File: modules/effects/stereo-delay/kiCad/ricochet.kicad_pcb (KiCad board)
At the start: 2 copper layers, 60 x 110 mm, 129 parts, among them J1 INPUT, J2 OUTPUT, J3 OUTPUT, J4 INPUT, Q1 2N3904, Q2 2N3904, U1 TL072, U2 PT2399, U3 PT2399, U4 TL074, U6 L7805

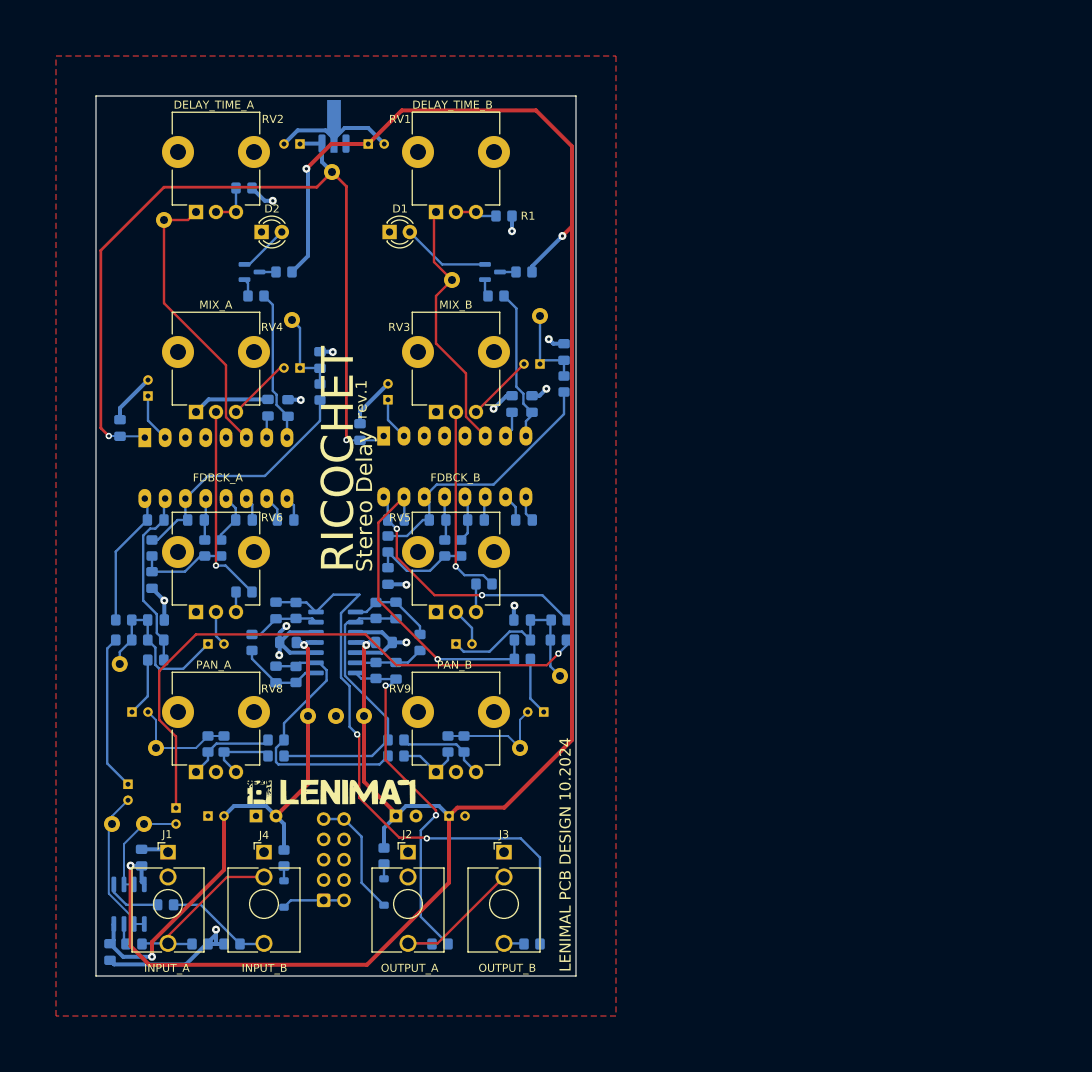
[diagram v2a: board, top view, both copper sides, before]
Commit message: debugging and rework for ricochet, midas, wolkje. Added IBOM for drums and other modules.
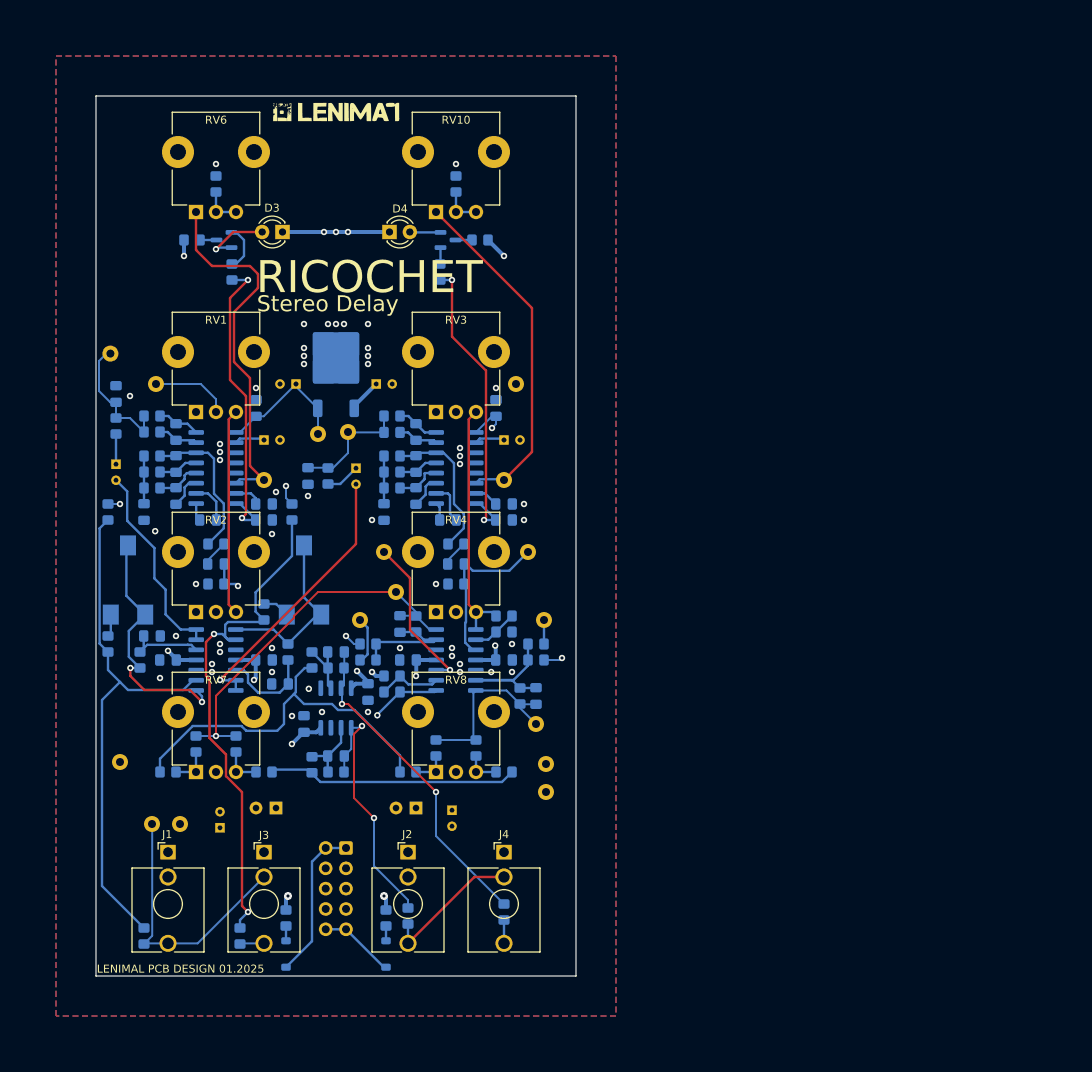
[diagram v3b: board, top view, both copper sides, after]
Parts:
- removed C43: 10uF, Capacitor_THT:CP_Radial_D4.0mm_P2.00mm
- removed C44: 4.7uF, Capacitor_THT:CP_Radial_D4.0mm_P2.00mm
- removed the G*** at (79.5, 137.0)
- added G***: LOGO, Synth:lenimal_logo_full, F.Cu at (80.1, 52.0)
- added G***: LOGO, Synth:lenimal_logo_full, B.Cu at (101.7, 51.5)
- added R47: 10K, Resistor_SMD:R_0805_2012Metric_Pad1.20x1.40mm_HandSolder, B.Cu at (55.5, 120.5)
- added R48: 10K, Resistor_SMD:R_0805_2012Metric_Pad1.20x1.40mm_HandSolder, B.Cu at (87.0, 90.0)
- added R49: 10K, Resistor_SMD:R_0805_2012Metric_Pad1.20x1.40mm_HandSolder, B.Cu at (87.0, 92.0)
- added R50: 10K, Resistor_SMD:R_0805_2012Metric_Pad1.20x1.40mm_HandSolder, B.Cu at (95.0, 106.0)
- added R51: 2K7, Resistor_SMD:R_0805_2012Metric_Pad1.20x1.40mm_HandSolder, B.Cu at (95.0, 61.0)
- added R52: 10K, Resistor_SMD:R_0805_2012Metric_Pad1.20x1.40mm_HandSolder, B.Cu at (87.0, 99.0)
- added R53: 10K, Resistor_SMD:R_0805_2012Metric_Pad1.20x1.40mm_HandSolder, B.Cu at (87.0, 97.0)
- added R54: 15K, Resistor_SMD:R_0805_2012Metric_Pad1.20x1.40mm_HandSolder, B.Cu at (87.0, 95.0)
- added R55: 1K, Resistor_SMD:R_0805_2012Metric_Pad1.20x1.40mm_HandSolder, B.Cu at (93.0, 72.0)
- added R56: 680R, Resistor_SMD:R_0805_2012Metric_Pad1.20x1.40mm_HandSolder, B.Cu at (98.0, 68.0)
- added RV10: B100K, Synth:Potentiometer_TT_P0915N, F.Cu at (95.0, 57.0)
- added RV7: B10K, Synth:Potentiometer_TT_P0915N, F.Cu at (65.0, 127.0)
- added TP15: -12V, Connector_Pin:Pin_D1.0mm_L10.0mm, B.Cu at (53.0, 133.2)
- added TP16: +5V, Connector_Pin:Pin_D1.0mm_L10.0mm, B.Cu at (77.8, 92.2)
- added TP17: DELAY_TIME, Connector_Pin:Pin_D1.0mm_L10.0mm, B.Cu at (71.0, 98.0)
- added TP18: DELAY_TIME, Connector_Pin:Pin_D1.0mm_L10.0mm, B.Cu at (101.0, 98.0)
- added U5: PT2399, Synth:SOIC-16, B.Cu at (65.0, 96.5)
- C1: value 10uF -> 1uF; footprint Capacitor_THT:CP_Radial_D4.0mm_P2.00mm -> Capacitor_SMD:C_0805_2012Metric_Pad1.18x1.45mm_HandSolder
- C10, C6, C7, C8: footprint Capacitor_SMD:C_0805_2012Metric_Pad1.18x1.45mm_HandSolder -> Capacitor_THT:CP_Radial_D4.0mm_P2.00mm
- C11, C13, C16: value 560pF -> 100nF
- C15, C20: value 4.7uF -> 100nF; footprint Capacitor_THT:CP_Radial_D4.0mm_P2.00mm -> Capacitor_SMD:C_0805_2012Metric_Pad1.18x1.45mm_HandSolder
- C17: value 4.7uF -> 1uF
- C18: value 560pF -> 1nF
- C19: value 3.3nF -> 2.2nF
- C2, C29, C30: value 100nF -> 47pF
- C21: value 10uF -> 560pF; footprint Capacitor_THT:CP_Radial_D4.0mm_P2.00mm -> Capacitor_SMD:C_0805_2012Metric_Pad1.18x1.45mm_HandSolder
- C22: value 3.3nF -> 1uF; footprint Capacitor_SMD:C_0805_2012Metric_Pad1.18x1.45mm_HandSolder -> Capacitor_THT:CP_Radial_D4.0mm_P2.00mm
- C23: value 10nF -> 2.2nF
- C24, C39: value 3.9nF -> 100nF
- C25, C26: value 27pF -> 100nF
- C27: value 47pF -> 100nF
- C28: value 47pF -> 3.3nF
- C3, C36: value 100nF -> 1uF
- C31: value 47uF -> 1uF; footprint Capacitor_THT:CP_Radial_D6.3mm_P2.50mm -> Capacitor_THT:CP_Radial_D4.0mm_P2.00mm
- C32: value 47uF -> 1nF; footprint Capacitor_THT:CP_Radial_D6.3mm_P2.50mm -> Capacitor_SMD:C_0805_2012Metric_Pad1.18x1.45mm_HandSolder
- C33: value 100nF -> 2.2nF
- C35: value 100nF -> 560pF; footprint Capacitor_THT:CP_Radial_D4.0mm_P2.00mm -> Capacitor_SMD:C_0805_2012Metric_Pad1.18x1.45mm_HandSolder
- C37: value 100nF -> 2.2nF; footprint Capacitor_THT:CP_Radial_D4.0mm_P2.00mm -> Capacitor_SMD:C_0805_2012Metric_Pad1.18x1.45mm_HandSolder
- C38: footprint Capacitor_THT:CP_Radial_D4.0mm_P2.00mm -> Capacitor_SMD:C_0805_2012Metric_Pad1.18x1.45mm_HandSolder
- C4: value 10uF -> 47pF; footprint Capacitor_THT:CP_Radial_D4.0mm_P2.00mm -> Capacitor_SMD:C_0805_2012Metric_Pad1.18x1.45mm_HandSolder
- C40: value 10nF -> 100nF
- C41: value 10uF -> 100nF; footprint Capacitor_THT:CP_Radial_D4.0mm_P2.00mm -> Capacitor_SMD:C_0805_2012Metric_Pad1.18x1.45mm_HandSolder
- C42: value 10uF -> 3.3nF; footprint Capacitor_THT:CP_Radial_D4.0mm_P2.00mm -> Capacitor_SMD:C_0805_2012Metric_Pad1.18x1.45mm_HandSolder
- C5, C9: value 100nF -> 47uF; footprint Capacitor_SMD:C_0805_2012Metric_Pad1.18x1.45mm_HandSolder -> Capacitor_THT:CP_Radial_D6.3mm_P2.50mm
- D1, D2: value LED -> 1N5819; footprint Synth:LED_D3.0mm -> Diode_SMD:D_SOD-123; moved to B.Cu
- D3, D4: value 1N5819 -> LED; footprint Diode_SMD:D_SOD-123 -> Synth:LED_D3.0mm; moved to F.Cu
- R1: value 2K -> 100K
- R10: value 15K -> 82K
- R12, R19: value 5.6K -> 100K
- R13: value 15K -> 100K
- R14, R17, R9: value 10K -> 100K
- R15, R16: value 10K -> 10R
- R18: value 4.7K -> 5K6
- R2: value 2K -> 82K
- R20, R21: value 15K -> 10K
- R23, R4: value 1K -> 10K
- R24: value 100K -> 10K
- R25: value 10K -> 2K7
- R27: value 4.7K -> 10K
- R28: value 10K -> 15K
- R29: value 10K -> 1K
- R30: value 10K -> 680R
- R37, R38: value 33K -> 10K
- R43, R5, R6: value 1K -> 100K
- R44: value 1K -> 5K6
- R45: value 10R -> 100K
- R46: value 10R -> 10K
- R7, R8: value 680R -> 1K
- RV1, RV2: value B50K -> B10K
- RV3, RV4: value B100K -> B10K
- RV5: value B100K -> 10K; footprint Synth:Potentiometer_TT_P0915N -> Potentiometer_SMD:Potentiometer_ACP_CA6-VSMD_Vertical; moved to B.Cu
- RV9: value B10K -> 10K; footprint Synth:Potentiometer_TT_P0915N -> Potentiometer_SMD:Potentiometer_ACP_CA6-VSMD_Vertical; moved to B.Cu
- TP1: value +12V -> FEEDBACK_A
- TP10: value POST_FEEDBACK_CH_2 -> OUTPUT_CH_1
- TP11: value POST_FEEDBACK_CH_1 -> MIXED_OUT_B
- TP12: value MIX_INPUT_CH_2 -> WET_OUT_B
- TP13: value MIX_INPUT_CH_1 -> +12V
- TP14: value +5V -> GND
- TP2: value GND -> DRY_A
- TP3: value -12V -> INPUT_CH_1
- TP4: value INPUT_CH_1 -> OUTPUT_CH_1
- TP5: value INPUT_CH_2 -> WET_OUT_A
- TP6: value OUTPUT_CH_1 -> FEEDBACK_B
- TP7: value OUTPUT_CH_2 -> MIXED_OUT_A
- TP8: value DELAY_TIME_CH_2 -> DRY_B
- TP9: value DELAY_TIME_CH_1 -> INPUT_CH_2
- U1: value TL072 -> TL074; footprint Synth:SOIC-8 -> Synth:SOIC-14
- U2: value PT2399 -> L7805; footprint Package_DIP:DIP-16_W7.62mm_Socket_LongPads -> Package_TO_SOT_SMD:TO-252-2
- U3: value PT2399 -> TL074; footprint Package_DIP:DIP-16_W7.62mm_Socket_LongPads -> Synth:SOIC-14
- U4: value TL074 -> TL072; footprint Synth:SOIC-14 -> Synth:SOIC-8
- U6: value L7805 -> PT2399; footprint Package_TO_SOT_SMD:SOT-89-3_Handsoldering -> Synth:SOIC-16
- moved D1 90.3 mm to (86.2, 157.2), turned to -90 degrees
- moved D2 90.3 mm to (73.8, 157.2), turned to 90 degrees
- moved R8 84.6 mm to (101.0, 152.0), turned to 90 degrees
- moved D4 84.0 mm to (88.0, 67.0), turned to 0 degrees
- moved D3 83.7 mm to (72.0, 67.0), turned to 180 degrees
- moved R7 81.8 mm to (89.0, 152.5), turned to 90 degrees
- moved TP14 78.7 mm to (106.2, 133.5)
- moved TP8 76.0 mm to (60.5, 141.0)
- moved R19 68.7 mm to (68.0, 155.0), turned to -90 degrees
- moved R43 68.1 mm to (51.5, 102.0), turned to 90 degrees
- moved TP13 67.0 mm to (106.2, 137.0)
- moved R2 65.7 mm to (87.0, 124.5), turned to 0 degrees
- moved R44 64.9 mm to (51.5, 118.5), turned to -90 degrees
- moved TP6 64.0 mm to (102.5, 86.0)
- moved R30 63.0 mm to (62.0, 68.0), turned to 180 degrees
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- renumbered J4 to J3, J3 to J4
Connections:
- C1 pad 1: Net-(U2-REF) -> /delay_stage_A/DELAY_OUT
- C1 pad 2: GNDREF -> Net-(U1C-+)
- C10 pad 1: Net-(U3-OP2-IN) -> GNDREF
- C10 pad 2: Net-(U3-OP2-OUT) -> -12V
- C11 pad 1: Net-(U2-LPF1-IN) -> +12V
- C11 pad 2: Net-(U2-LPF1-OUT) -> GNDREF
- C12 pad 1: Net-(U3-OP1-IN) -> +12V
- C12 pad 2: Net-(U3-OP1-OUT) -> GNDREF
- C13 pad 1: Net-(U2-LPF2-OUT) -> +12V
- C13 pad 2: Net-(U2-LPF2-IN) -> GNDREF
- C14 pad 1: Net-(U2-OP2-IN) -> GNDREF
- C14 pad 2: Net-(U2-OP2-OUT) -> -12V
- C15 pad 1: Net-(C15-Pad1) -> GNDREF
- C15 pad 2: /PT2399_delay-module_channel_1/delay_input -> -12V
- C16 pad 1: Net-(U3-LPF1-IN) -> GNDREF
- C16 pad 2: Net-(U3-LPF1-OUT) -> -12V
- C17 pad 2: /PT2399_delay-module_channel_2/delay_input -> Net-(U3B--)
- C18 pad 1: Net-(U3-LPF2-OUT) -> GNDREF
- C18 pad 2: Net-(U3-LPF2-IN) -> /delay_stage_B/DELAY_IN
- C19 pad 1: Net-(C19-Pad1) -> GNDREF
- C19 pad 2: GNDREF -> Net-(U3B-+)
- C2 pad 1: GNDREF -> Net-(U1D--)
- C2 pad 2: +5V -> /panning/INPUT_A
- C20 pad 1: Net-(C20-Pad1) -> GNDREF
- C20 pad 2: Net-(C20-Pad2) -> +5V
- C21 pad 1: Net-(C21-Pad1) -> Net-(U5-LPF1-IN)
- C21 pad 2: Net-(C21-Pad2) -> Net-(U5-LPF1-OUT)
- C22 pad 1: Net-(C22-Pad1) -> Net-(U5-REF)
- C23 pad 1: Net-(C23-Pad1) -> Net-(U5-LPF2-OUT)
- C23 pad 2: GNDREF -> Net-(U5-LPF2-IN)
- C24 pad 1: Net-(C24-Pad1) -> Net-(U5-OP2-OUT)
- C24 pad 2: GNDREF -> Net-(U5-OP2-IN)
- C25 pad 1: Net-(U4A--) -> GNDREF
- C25 pad 2: Net-(C25-Pad2) -> Net-(U5-CC1)
- C26 pad 1: Net-(U4C--) -> Net-(U5-CC0)
- C26 pad 2: Net-(C26-Pad2) -> GNDREF
- C27 pad 1: Net-(U4B--) -> Net-(U5-OP1-IN)
- C27 pad 2: Net-(C27-Pad2) -> Net-(U5-OP1-OUT)
- C28 pad 1: Net-(U4D--) -> Net-(C28-Pad1)
- C28 pad 2: Net-(C28-Pad2) -> GNDREF
- C29 pad 1: +12V -> Net-(U4A--)
- C29 pad 2: GNDREF -> /panning/OUTPUT_A
- C3 pad 1: Net-(U2-CC1) -> /delay_stage_B/DELAY_OUT
- C3 pad 2: GNDREF -> Net-(U1A-+)
- C30 pad 1: GNDREF -> Net-(U4B--)
- C30 pad 2: -12V -> /panning/OUTPUT_B
- C31 pad 1: +12V -> Net-(C31-Pad1)
- C31 pad 2: GNDREF -> Net-(U3D--)
- C32 pad 2: -12V -> /delay_stage_A/DELAY_IN
- C33 pad 1: +12V -> GNDREF
- C33 pad 2: GNDREF -> Net-(U3D-+)
- C34 pad 2: -12V -> +5V
- C35 pad 1: +12V -> Net-(U6-LPF1-IN)
- C35 pad 2: GNDREF -> Net-(U6-LPF1-OUT)
- C36 pad 1: GNDREF -> Net-(U6-REF)
- C36 pad 2: -12V -> GNDREF
- C37 pad 1: +12V -> Net-(U6-LPF2-OUT)
- C37 pad 2: GNDREF -> Net-(U6-LPF2-IN)
- C38 pad 1: +5V -> Net-(U6-OP2-OUT)
- C38 pad 2: GNDREF -> Net-(U6-OP2-IN)
- C39 pad 1: Net-(C20-Pad1) -> GNDREF
- C39 pad 2: GNDREF -> Net-(U6-CC1)
- C4 pad 1: Net-(U3-REF) -> Net-(U1B--)
- C4 pad 2: GNDREF -> /panning/INPUT_B
- C40 pad 1: Net-(C21-Pad1) -> Net-(U6-CC0)
- C41 pad 1: Net-(C41-Pad1) -> Net-(U6-OP1-IN)
- C41 pad 2: /PT2399_delay-module_channel_2/delay_output -> Net-(U6-OP1-OUT)
- C42 pad 2: /PT2399_delay-module_channel_1/delay_output -> GNDREF
- C5 pad 1: Net-(U2-CC0) -> +12V
- C6 pad 1: +5V -> +12V
- C7 pad 1: Net-(U3-CC1) -> +12V
- C8 pad 1: Net-(U3-CC0) -> +5V
- C9 pad 1: Net-(U2-OP1-IN) -> GNDREF
- C9 pad 2: Net-(U2-OP1-OUT) -> -12V
- D1 pad 1: GNDREF -> Net-(D1-K)
- D2 pad 1: GNDREF -> Net-(D2-K)
- D3 pad 1: Net-(D3-K) -> GNDREF
- D4 pad 1: Net-(D4-K) -> GNDREF
- H1 pad 1: Net-(D4-K) -> Net-(D2-K)
- H1 pad 10: Net-(D3-A) -> Net-(D1-A)
- H1 pad 2: Net-(D4-K) -> Net-(D2-K)
- H1 pad 9: Net-(D3-A) -> Net-(D1-A)
- J1 pad T: Net-(J1-PadT) -> /input_stage_A/DRY_IN
- J3 pad T: Net-(J4-PadT) -> /input_stage_B/DRY_IN
- J3 pad TN: Net-(J1-PadT) -> /input_stage_A/DRY_IN
- J4 pad T: Net-(J3-PadT) -> Net-(J4-PadT)
- Q1 pad 2: Net-(D1-A) -> Net-(D3-A)
- Q2 pad 2: Net-(D2-A) -> Net-(D4-A)
- R1 pad 2: Net-(R1-Pad2) -> Net-(U1C-+)
- R10 pad 1: Net-(C15-Pad1) -> Net-(U1A--)
- R10 pad 2: Net-(C24-Pad1) -> Net-(R10-Pad2)
- R11 pad 1: Net-(U2-LPF1-OUT) -> GNDREF
- R11 pad 2: Net-(C20-Pad1) -> Net-(U1A--)
- R12 pad 1: Net-(U2-LPF2-OUT) -> Net-(U1B--)
- R12 pad 2: Net-(C21-Pad1) -> /panning/INPUT_B
- R13 pad 1: Net-(U2-LPF2-OUT) -> Net-(R13-Pad1)
- R13 pad 2: Net-(C19-Pad1) -> Net-(U1B--)
- R14 pad 1: Net-(U2-LPF2-IN) -> /input_stage_B/DRY_IN
- R14 pad 2: Net-(C19-Pad1) -> Net-(U1B--)
- R15 pad 1: Net-(U2-OP2-OUT) -> Net-(D1-K)
- R15 pad 2: Net-(C19-Pad1) -> +12V
- R16 pad 1: Net-(U3-LPF1-IN) -> Net-(D2-A)
- R16 pad 2: Net-(C24-Pad1) -> -12V
- R17 pad 1: Net-(U3-LPF1-OUT) -> Net-(U3A--)
- R17 pad 2: Net-(C24-Pad1) -> /input_stage_B/FEEDBACKIN_IN
- R18 pad 1: Net-(U3-LPF1-OUT) -> Net-(R18-Pad1)
- R18 pad 2: Net-(C42-Pad1) -> Net-(U3A--)
- R19 pad 1: Net-(U3-LPF2-OUT) -> Net-(U3A--)
- R19 pad 2: Net-(C23-Pad1) -> /input_stage_B/DRY_IN
- R2 pad 1: GNDREF -> Net-(U1C--)
- R20 pad 1: Net-(U3-LPF2-OUT) -> Net-(C17-Pad1)
- R20 pad 2: Net-(C22-Pad1) -> /delay_stage_B/DELAY_IN
- R21 pad 1: Net-(C17-Pad1) -> Net-(U3B-+)
- R21 pad 2: Net-(C20-Pad1) -> Net-(R21-Pad2)
- R22 pad 1: Net-(U3-LPF2-IN) -> /delay_stage_A/DELAY_IN
- R22 pad 2: Net-(C22-Pad1) -> Net-(U5-LPF1-IN)
- R23 pad 1: Net-(U1B-+) -> /delay_stage_A/DELAY_IN
- R23 pad 2: Net-(J4-PadT) -> Net-(U5-LPF1-OUT)
- R24 pad 1: GNDREF -> Net-(U5-LPF2-OUT)
- R24 pad 2: Net-(J4-PadT) -> /delay_stage_A/DELAY_OUT
- R25 pad 1: Net-(R25-Pad1) -> GNDREF
- R26 pad 1: Net-(U3-OP2-OUT) -> Net-(C28-Pad1)
- R26 pad 2: Net-(C22-Pad1) -> Net-(U5-OP2-OUT)
- R27 pad 1: Net-(U2-LPF1-OUT) -> Net-(C28-Pad1)
- R27 pad 2: Net-(C41-Pad1) -> Net-(U5-LPF2-IN)
- R28 pad 1: Net-(R28-Pad1) -> Net-(C28-Pad1)
- R28 pad 2: Net-(R28-Pad2) -> Net-(U5-LPF2-OUT)
- R29 pad 1: /PT2399_delay-module_channel_1/delay_output -> Net-(U5-CC0)
- R29 pad 2: Net-(R29-Pad2) -> Net-(Q1-B)
- R3 pad 1: GNDREF -> Net-(U1D--)
- R3 pad 2: Net-(J1-PadT) -> /panning/INPUT_A
- R30 pad 1: /PT2399_delay-module_channel_1/delay_output -> Net-(Q1-C)
- R30 pad 2: Net-(R30-Pad2) -> +12V
- R31 pad 1: /PT2399_delay-module_channel_2/delay_output -> Net-(U4A--)
- R31 pad 2: Net-(R31-Pad2) -> /panning/OUTPUT_A
- R32 pad 1: /PT2399_delay-module_channel_2/delay_output -> /panning/INPUT_A
- R33 pad 1: Net-(R29-Pad2) -> Net-(R32-Pad2)
- R33 pad 2: Net-(U4A--) -> Net-(R33-Pad2)
- R34 pad 1: Net-(R30-Pad2) -> Net-(R33-Pad2)
- R34 pad 2: Net-(U4C--) -> Net-(U4A--)
- R35 pad 1: Net-(R31-Pad2) -> /panning/INPUT_A
- R35 pad 2: Net-(U4A--) -> Net-(R35-Pad2)
- R36 pad 1: Net-(R32-Pad2) -> Net-(R36-Pad1)
- R36 pad 2: Net-(U4C--) -> Net-(R35-Pad2)
- R37 pad 1: Net-(U4A--) -> /panning/INPUT_B
- R37 pad 2: Net-(C25-Pad2) -> Net-(R37-Pad2)
- R38 pad 1: Net-(U4C--) -> Net-(R37-Pad2)
- R38 pad 2: Net-(C26-Pad2) -> Net-(R33-Pad2)
- R39 pad 1: Net-(C25-Pad2) -> Net-(U4B--)
- R39 pad 2: Net-(U4B--) -> /panning/OUTPUT_B
- R4 pad 1: Net-(U1A-+) -> GNDREF
- R4 pad 2: Net-(J1-PadT) -> Net-(U1C--)
- R40 pad 1: Net-(C26-Pad2) -> /panning/INPUT_B
- R40 pad 2: Net-(U4D--) -> Net-(R40-Pad2)
- R41 pad 1: Net-(U4B--) -> Net-(R40-Pad2)
- R41 pad 2: Net-(C27-Pad2) -> Net-(R36-Pad1)
- R42 pad 1: Net-(U4D--) -> Net-(R36-Pad1)
- R42 pad 2: Net-(C28-Pad2) -> Net-(U4B--)
- R43 pad 1: Net-(J2-PadT) -> Net-(U3C--)
- R43 pad 2: Net-(C27-Pad2) -> /input_stage_A/FEEDBACKIN_IN
- R44 pad 1: Net-(J3-PadT) -> Net-(R44-Pad1)
- R44 pad 2: Net-(C28-Pad2) -> Net-(U3C--)
- R45 pad 1: Net-(D3-K) -> Net-(U3C--)
- R45 pad 2: +12V -> /input_stage_A/DRY_IN
- R46 pad 1: Net-(D4-A) -> Net-(C31-Pad1)
- R46 pad 2: -12V -> /delay_stage_A/DELAY_IN
- R5 pad 1: Net-(U2-CC0) -> Net-(R5-Pad1)
- R5 pad 2: Net-(Q1-B) -> Net-(U1D--)
- R6 pad 1: Net-(U3-CC0) -> /input_stage_A/DRY_IN
- R6 pad 2: Net-(Q2-B) -> Net-(U1D--)
- R7 pad 1: Net-(Q1-C) -> Net-(J2-PadT)
- R7 pad 2: +12V -> /panning/OUTPUT_A
- R8 pad 1: Net-(Q2-C) -> Net-(J4-PadT)
- R8 pad 2: +12V -> /panning/OUTPUT_B
- R9 pad 1: Net-(U2-LPF1-IN) -> GNDREF
- R9 pad 2: Net-(C20-Pad1) -> Net-(U1A-+)
- RV1 pad 1: Net-(U2-VCO) -> GNDREF
- RV1 pad 2: Net-(R1-Pad2) -> /input_stage_A/FEEDBACKIN_IN
- RV1 pad 3: Net-(R1-Pad2) -> Net-(R2-Pad2)
- RV2 pad 1: Net-(U3-VCO) -> GNDREF
- RV2 pad 2: Net-(R2-Pad2) -> Net-(R5-Pad1)
- RV3 pad 2: Net-(R25-Pad2) -> /input_stage_B/FEEDBACKIN_IN
- RV3 pad 3: Net-(C21-Pad2) -> Net-(R10-Pad2)
- RV4 pad 2: Net-(R28-Pad2) -> Net-(R13-Pad1)
- RV4 pad 3: Net-(C43-Pad2) -> Net-(R10-Pad2)
- RV5 pad 1: unconnected-(RV5-Pad1) -> Net-(R18-Pad1)
- RV5 pad 2: Net-(C20-Pad2) -> Net-(R21-Pad2)
- RV5 pad 3: Net-(R25-Pad1) -> Net-(R21-Pad2)
- RV6 pad 1: unconnected-(RV6-Pad1) -> Net-(U5-VCO)
- RV6 pad 2: Net-(C44-Pad2) -> Net-(R25-Pad2)
- RV6 pad 3: Net-(R28-Pad1) -> Net-(R25-Pad2)
- RV8 pad 1: Net-(R30-Pad2) -> Net-(R40-Pad2)
- RV8 pad 3: Net-(R29-Pad2) -> Net-(R37-Pad2)
- RV9 pad 1: Net-(R32-Pad2) -> Net-(R44-Pad1)
- RV9 pad 2: GNDREF -> Net-(R47-Pad2)
- RV9 pad 3: Net-(R31-Pad2) -> Net-(R47-Pad2)
- TP1 pad 1: +12V -> /input_stage_A/FEEDBACKIN_IN
- TP10 pad 1: Net-(C20-Pad1) -> Net-(U1A-+)
- TP11 pad 1: Net-(C24-Pad1) -> /panning/INPUT_B
- TP12 pad 1: Net-(C21-Pad1) -> Net-(R13-Pad1)
- TP13 pad 1: Net-(C23-Pad1) -> +12V
- TP14 pad 1: +5V -> GNDREF
- TP2 pad 1: GNDREF -> /input_stage_A/DRY_IN
- TP3 pad 1: -12V -> /delay_stage_A/DELAY_IN
- TP4 pad 1: /PT2399_delay-module_channel_1/delay_input -> Net-(U1C-+)
- TP5 pad 1: /PT2399_delay-module_channel_2/delay_input -> Net-(R5-Pad1)
- TP6 pad 1: /PT2399_delay-module_channel_1/delay_output -> /input_stage_B/FEEDBACKIN_IN
- TP7 pad 1: /PT2399_delay-module_channel_2/delay_output -> /panning/INPUT_A
- TP8 pad 1: Net-(U2-VCO) -> /input_stage_B/DRY_IN
- TP9 pad 1: Net-(U3-VCO) -> /delay_stage_B/DELAY_IN
- U1 pad 1: /PT2399_delay-module_channel_1/delay_input -> Net-(R10-Pad2)
- U1 pad 2: /PT2399_delay-module_channel_1/delay_input -> Net-(U1A--)
- U1 pad 4: -12V -> +12V
- U1 pad 5: Net-(U1B-+) -> GNDREF
- U1 pad 6: /PT2399_delay-module_channel_2/delay_input -> Net-(U1B--)
- U1 pad 7: /PT2399_delay-module_channel_2/delay_input -> /panning/INPUT_B
- U1 pad 8: +12V -> Net-(R2-Pad2)
- U2 pad 1: +5V -> +12V
- U2 pad 2: Net-(U2-REF) -> GNDREF
- U2 pad 3: GNDREF -> +5V
- U3 pad 1: +5V -> Net-(R21-Pad2)
- U3 pad 10: Net-(U3-OP1-IN) -> GNDREF
- U3 pad 11: Net-(U3-OP2-IN) -> -12V
- U3 pad 12: Net-(U3-OP2-OUT) -> Net-(U3D-+)
- U3 pad 13: Net-(U3-LPF2-IN) -> Net-(U3D--)
- U3 pad 14: Net-(U3-LPF2-OUT) -> Net-(U3D--)
- U3 pad 2: Net-(U3-REF) -> Net-(U3A--)
- U3 pad 4: GNDREF -> +12V
- U3 pad 5: unconnected-(U3-CLK_O-Pad5) -> Net-(U3B-+)
- U3 pad 6: Net-(U3-VCO) -> Net-(U3B--)
- U3 pad 7: Net-(U3-CC1) -> Net-(U3B--)
- U3 pad 8: Net-(U3-CC0) -> Net-(R47-Pad2)
- U3 pad 9: Net-(U3-OP1-OUT) -> Net-(U3C--)
- U4 pad 1: Net-(C25-Pad2) -> /panning/OUTPUT_A
- U4 pad 4: +12V -> -12V
- U4 pad 7: Net-(C27-Pad2) -> /panning/OUTPUT_B
- U4 pad 8: Net-(C26-Pad2) -> +12V
- U6 pad 1: +12V -> +5V
- U6 pad 2: GNDREF -> Net-(U6-REF)
- U6 pad 3: +5V -> GNDREF
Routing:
- net /input_stage_B/DRY_IN: track 0.00 -> 103.0 mm, vias 0 -> 1
- net GNDREF: track 111.5 -> 15.1 mm, vias 14 -> 55
- net /input_stage_A/DRY_IN: track 0.00 -> 92.0 mm, vias 0 -> 1
- net Net-(C28-Pad2): track 75.6 -> 0.00 mm, vias 2 -> 0
- net Net-(C17-Pad1): track 74.1 -> 4.32 mm, vias 1 -> 0
- net Net-(U3C--): track 0.00 -> 66.0 mm
- net Net-(U3A--): track 0.00 -> 64.7 mm, vias 0 -> 2
- net Net-(R2-Pad2): track 5.50 -> 64.6 mm, vias 0 -> 1
- net +5V: track 107.1 -> 49.2 mm, vias 2 -> 1
- net /panning/INPUT_A: track 0.00 -> 47.3 mm, vias 0 -> 1
- net Net-(R36-Pad1): track 0.00 -> 46.9 mm
- net Net-(U5-VCO): track 0.00 -> 46.1 mm
- net Net-(U1C-+): track 0.00 -> 44.3 mm, vias 0 -> 2
- net Net-(C27-Pad2): track 44.1 -> 0.00 mm, vias 2 -> 0
- net Net-(U6-VCO): track 0.00 -> 43.7 mm
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- added copper zone on B.Cu, net GNDREF
- added copper zone on In1.Cu, net GNDREF
- added copper zone on In2.Cu, net GNDREF
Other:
- copper layers 2 -> 4
- board text added: "+12V"
- board text added: "-12V"
- board text added: "A_AMT"
- board text added: "B_AMT"
- board text added: "DLY_A"
- board text added: "DLY_B"
- board text added: "DLY_IN_A"
- board text added: "DLY_IN_B"
- board text added: "DRY_A"
- board text added: "DRY_B"
- board text added: "FBK_A"
- board text added: "FBK_B"
- board text added: "GND"
- board text added: "LENIMAL PCB DESIGN 01.2025"
- board text added: "WET_A"
- board text added: "WET_B"
- board text removed: "DELAY_TIME"
- board text removed: "DELAY_TIME_A"
- board text removed: "DELAY_TIME_B"
- board text removed: "DLY_IN"
- board text removed: "DLY_OUT"
- board text removed: "FDBCK"
- board text removed: "FDBCK_A"
- board text removed: "FDBCK_B"
- board text removed: "INPUT_A"
- board text removed: "INPUT_B"
- board text removed: "L7805"
- board text removed: "LENIMAL PCB DESIGN 10.2024"
- board text removed: "MIX"
- board text removed: "OUTPUT_A"
- board text removed: "OUTPUT_B"
- board text removed: "PAN_A"
- board text removed: "PAN_B"
- board text removed: "PT2399"
- board text removed: "TL072"
- board text removed: "TL074"
- board text removed: "rev.1"

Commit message: Add: Quantizer init, Fix: Stereo-Delay, Fix: Midi-2-xc
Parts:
- C18, C32: value 1nF -> 4.7nF
- C7, C8: value 100nF -> 10uF
- R13, R5: value 100K -> 68K
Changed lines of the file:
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@@
 			)
 		)
-		(property "Value" "100nF"
+		(property "Value" "10uF"
 			(at 1 -3.25 0)
 			(layer "B.Fab")
@@
 			)
 		)
-		(property "Value" "100nF"
+		(property "Value" "10uF"
 			(at 1 -3.25 0)
 			(layer "B.Fab")
@@
 			)
 		)
-		(property "Value" "1nF"
+		(property "Value" "4.7nF"
 			(at 0 -1.68 90)
 			(layer "B.Fab")
@@
 			)
 		)
-		(property "Value" "100K"
+		(property "Value" "68K"
 			(at 0 -1.65 0)
 			(layer "B.Fab")
@@
 			)
 		)
-		(property "Value" "100K"
+		(property "Value" "68K"
 			(at 0 -1.65 0)
 			(layer "B.Fab")
@@
 			)
 		)
-		(property "Value" "1nF"
+		(property "Value" "4.7nF"
 			(at 0 -1.68 90)
 			(layer "B.Fab")
